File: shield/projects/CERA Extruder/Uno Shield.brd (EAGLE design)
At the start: 55.9 x 53.3 mm, 5 parts

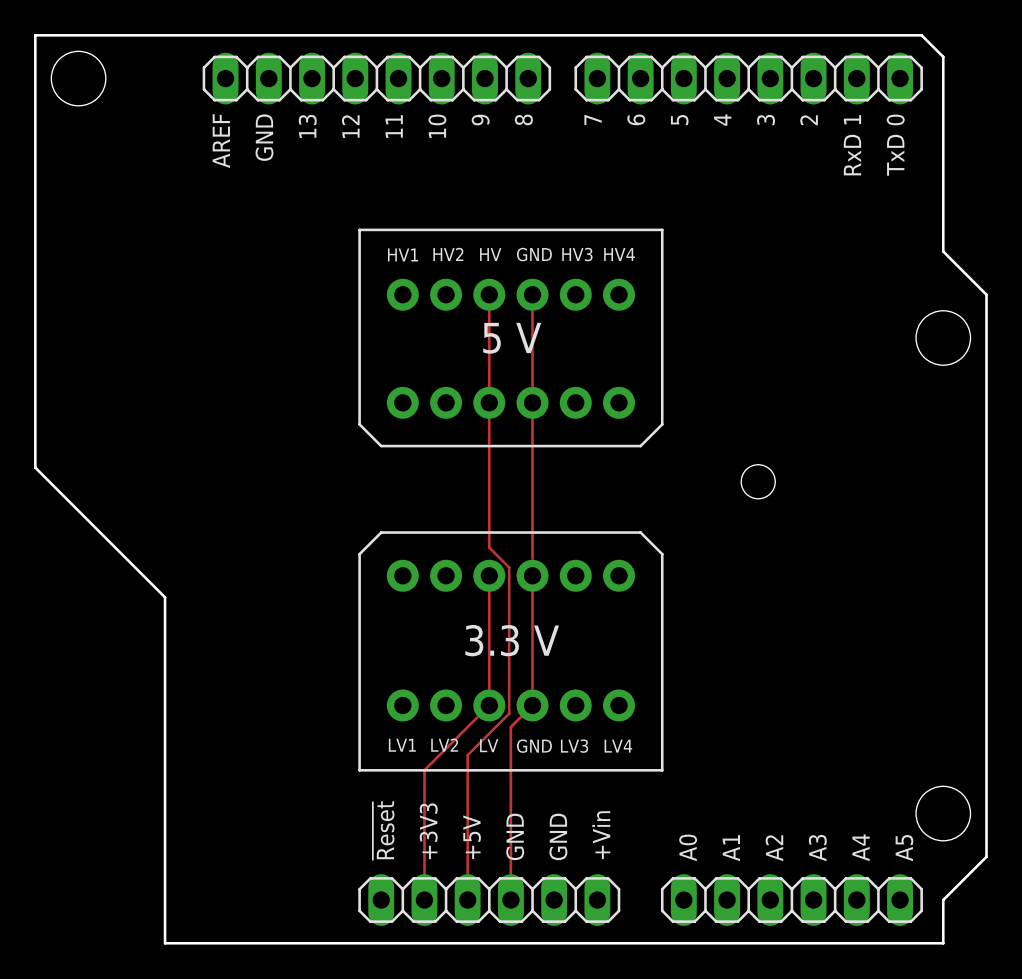
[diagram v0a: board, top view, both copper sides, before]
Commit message: compressed level shifter area on Uno shield
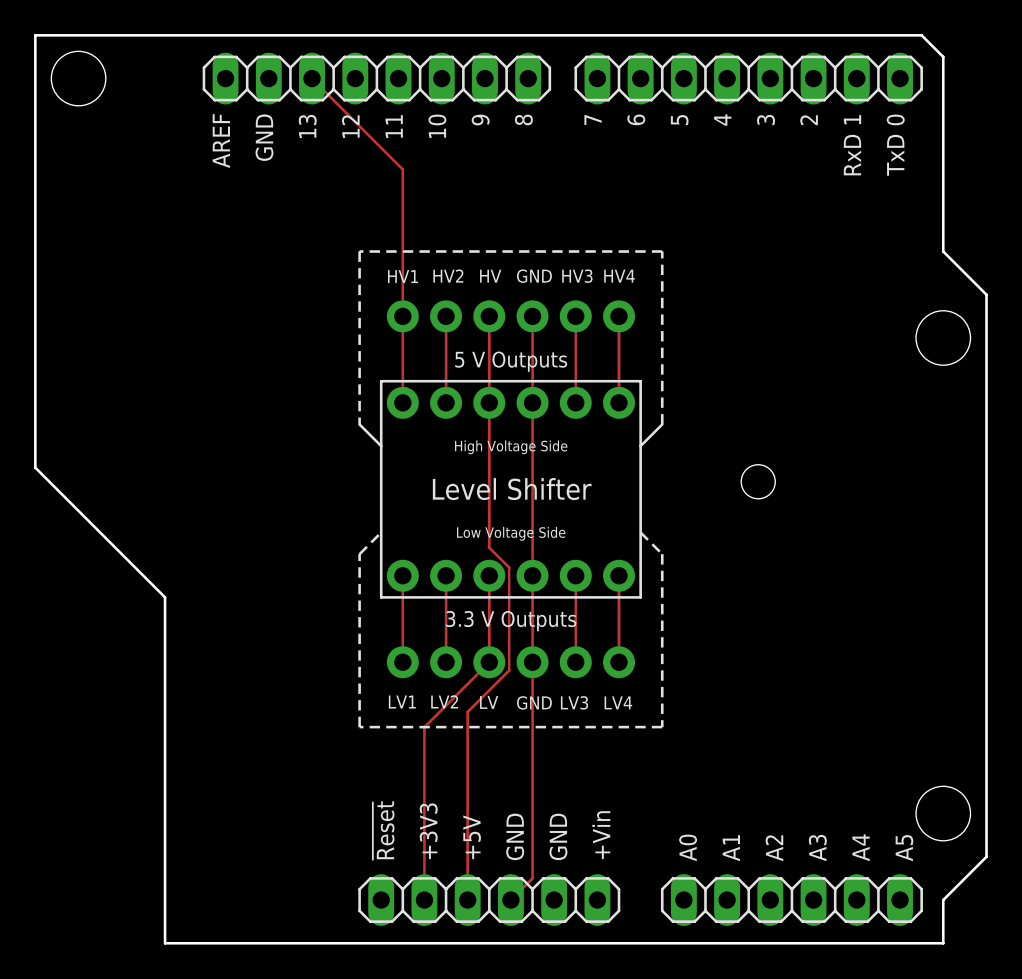
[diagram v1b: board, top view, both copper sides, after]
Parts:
- moved JP3 2.54 mm to (47.0, 16.5)
- moved JP4 1.27 mm to (34.3, 36.8)
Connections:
- new net S$10: JP1.6, JP3.6
- new net S$4: E$1.4, JP1.3, JP2.4, JP3.3, JP4.4
- new net S$5: E$1.3, JP2.3, JP4.3
- new net S$6: JP2.5, JP4.5
- new net S$7: JP2.6, JP4.6
- new net S$8: JP1.1, JP3.1
- new net S$9: JP1.2, JP3.2
- net LV2: now also JP3.5
- net S$2: now also E$1.26, JP2.1, JP4.1; no longer E$1.4, JP1.3, JP2.4, JP3.3, JP4.4
- net S$3: now also JP2.2, JP4.2; no longer E$1.3, JP2.3, JP4.3
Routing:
- net S$5: track 0.00 -> 35.8 mm
- net S$4: track 0.00 -> 34.8 mm
- net S$3: track 37.1 -> 5.08 mm
- net S$2: track 36.1 -> 21.3 mm
- net S$9: track 0.00 -> 5.08 mm
- net S$8: track 0.00 -> 5.08 mm
- net S$7: track 0.00 -> 5.08 mm
- net S$6: track 0.00 -> 5.08 mm
- net S$10: track 0.00 -> 5.08 mm
- net LV2: track 0.42 -> 5.50 mm
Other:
- board text added: "3.3 V Outputs"
- board text added: "5 V Outputs"
- board text added: "High Voltage Side"
- board text added: "Level Shifter"
- board text added: "Low Voltage Side"
- board text removed: "3.3 V"
- board text removed: "5 V"
